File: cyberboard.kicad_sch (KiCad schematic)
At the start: 21 parts, among them J2 Conn_01x06, J4 Lidar, J5 LED, J6 RPi_GPIO, J7 Conn_01x04, J8 Conn_01x03, Q4 AO3400A, U6 ESP32-S3-WROOM-1

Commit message: fix bugs
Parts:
- removed J5: LED, Connector_JST:JST_XH_B3B-XH-A_1x03_P2.50mm_Vertical, symbol Connector_Generic:Conn_01x03
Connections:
- net +3.3V: no longer J6.1 (3.3V), J6.17 (3.3V)
- net CAN_TX: now also U6.17 (GPIO9/TOUCH9/ADC1_CH8/FSPIHD/SUBSPIHD); no longer U6.12 (GPIO8/TOUCH8/ADC1_CH7/SUBSPICS1)
- net FAN: now also J6.8 (BCM14_TXD); no longer J6.11 (BCM17)
- net GPIO_LED: now also U6.12 (GPIO8/TOUCH8/ADC1_CH7/SUBSPICS1); no longer U6.17 (GPIO9/TOUCH9/ADC1_CH8/FSPIHD/SUBSPIHD)
- net MOTORCTL: now also J6.35 (BCM19_MISO_PCM_FS); no longer U6.9 (GPIO16/U0CTS/ADC2_CH5/XTAL_32K_N)
- net UART3_RX: now also U6.37 (U0TXD/GPIO43/CLK_OUT1); no longer U6.36 (U0RXD/GPIO44/CLK_OUT2)
- net UART3_TX: now also U6.36 (U0RXD/GPIO44/CLK_OUT2); no longer U6.37 (U0TXD/GPIO43/CLK_OUT1)
- no-connect marks 16 -> 17
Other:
- moved on the sheet: D1

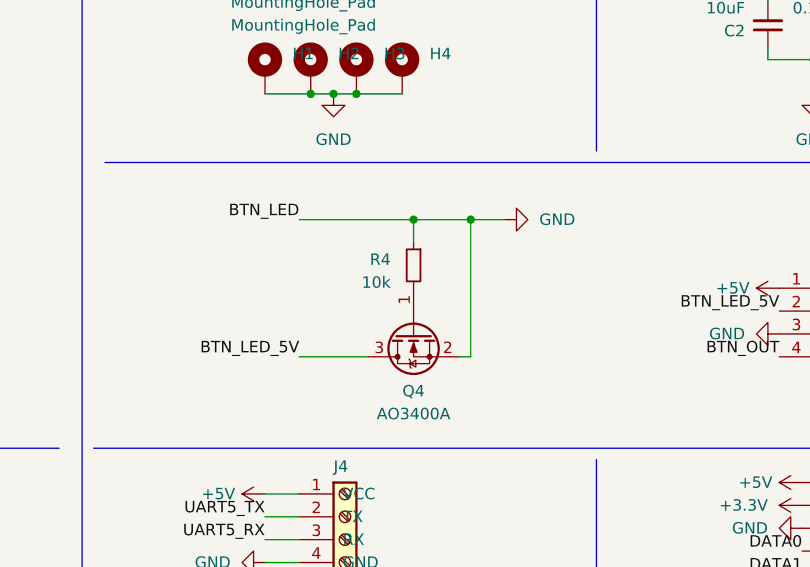
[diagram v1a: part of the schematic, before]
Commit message: fix BTN mosfet connection
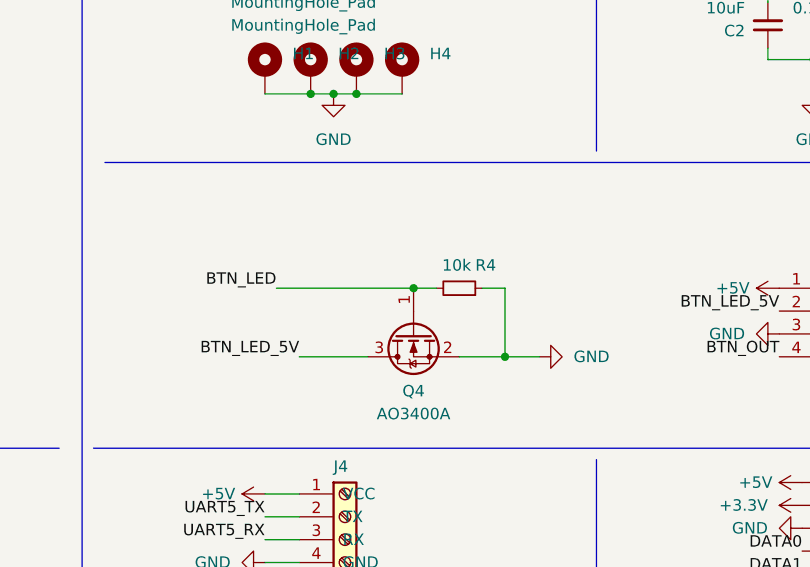
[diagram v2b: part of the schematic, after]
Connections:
- net GND: no longer U6.5 (GPIO5/TOUCH5/ADC1_CH4)
- net BTN_LED: now reaches Q4.1 (G), R4.2
- net BTN_LED: now also U6.5 (GPIO5/TOUCH5/ADC1_CH4)
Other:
- moved on the sheet: R4
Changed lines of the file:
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@@
 	(paper "A4")
 	(junction
-		(at 213.36 95.25)
+		(at 213.36 102.87)
 		(diameter 0)
 		(color 0 0 0 0)
@@
 	)
 	(junction
+		(at 223.52 110.49)
+		(diameter 0)
+		(color 0 0 0 0)
+	)
+	(junction
 		(at 201.93 81.28)
 		(diameter 0)
@@
 		(color 0 0 0 0)
 	)
-	(junction
-		(at 219.71 95.25)
-		(diameter 0)
-		(color 0 0 0 0)
-	)
 	(no_connect
 		(at 142.24 95.25)
@@
 	(wire
 		(pts
+			(xy 215.9 102.87) (xy 213.36 102.87)
+		)
+		(stroke
+			(width 0)
+			(type default)
+		)
+	)
+	(wire
+		(pts
 			(xy 196.85 130.81) (xy 200.66 130.81)
 		)
@@
 	(wire
 		(pts
+			(xy 198.12 102.87) (xy 213.36 102.87)
+		)
+		(stroke
+			(width 0)
+			(type default)
+		)
+	)
+	(wire
+		(pts
 			(xy 252.73 68.58) (xy 252.73 71.12)
 		)
@@
 		)
 	)
+	(wire
+		(pts
+			(xy 223.52 110.49) (xy 227.33 110.49)
+		)
+		(stroke
+			(width 0)
+			(type default)
+		)
+	)
 	(polyline
 		(pts
@@
 	(wire
 		(pts
-			(xy 213.36 95.25) (xy 213.36 97.79)
+			(xy 142.24 29.21) (xy 146.05 29.21)
 		)
 		(stroke
@@
 	(wire
 		(pts
-			(xy 142.24 29.21) (xy 146.05 29.21)
+			(xy 196.85 133.35) (xy 200.66 133.35)
 		)
 		(stroke
@@
 	(wire
 		(pts
-			(xy 196.85 133.35) (xy 200.66 133.35)
+			(xy 220.98 102.87) (xy 223.52 102.87)
 		)
 		(stroke
@@
 		)
 	)
-	(wire
-		(pts
-			(xy 219.71 95.25) (xy 219.71 110.49)
-		)
-		(stroke
-			(width 0)
-			(type default)
-		)
-	)
 	(polyline
 		(pts
@@
 	(wire
 		(pts
-			(xy 257.81 77.47) (xy 257.81 81.28)
+			(xy 223.52 102.87) (xy 223.52 110.49)
 		)
 		(stroke
@@
 	(wire
 		(pts
-			(xy 200.66 95.25) (xy 213.36 95.25)
+			(xy 257.81 77.47) (xy 257.81 81.28)
 		)
 		(stroke
@@
 	(wire
 		(pts
-			(xy 213.36 95.25) (xy 219.71 95.25)
-		)
-		(stroke
-			(width 0)
-			(type default)
-		)
-	)
-	(wire
-		(pts
 			(xy 87.63 142.24) (xy 96.52 142.24)
 		)
@@
 	(wire
 		(pts
-			(xy 218.44 110.49) (xy 219.71 110.49)
-		)
-		(stroke
-			(width 0)
-			(type default)
-		)
-	)
-	(wire
-		(pts
 			(xy 204.47 81.28) (xy 207.01 81.28)
 		)
@@
 	(wire
 		(pts
-			(xy 219.71 95.25) (xy 223.52 95.25)
+			(xy 218.44 110.49) (xy 223.52 110.49)
 		)
 		(stroke
@@
 	)
 	(label "BTN_LED"
-		(at 200.66 95.25 180)
+		(at 198.12 102.87 180)
 		(fields_autoplaced yes)
 		(effects
@@
 	(symbol
 		(lib_id "Device:R_Small")
-		(at 213.36 100.33 0)
-		(mirror y)
+		(at 218.44 102.87 270)
+		(mirror x)
 		(unit 1)
 		(exclude_from_sim no)
@@
 		(dnp no)
 		(property "Reference" "R4"
-			(at 210.82 99.695 0)
+			(at 220.218 100.33 90)
 			(effects
 				(font
@@
 		)
 		(property "Value" "10k"
-			(at 210.82 102.235 0)
+			(at 216.535 100.33 90)
 			(effects
 				(font
@@
 		)
 		(property "Footprint" "Resistor_SMD:R_0805_2012Metric"
-			(at 213.36 100.33 0)
+			(at 218.44 102.87 0)
 			(effects
 				(font
@@
 		)
 		(property "Datasheet" "~"
-			(at 213.36 100.33 0)
+			(at 218.44 102.87 0)
 			(effects
 				(font
@@
 		)
 		(property "Description" ""
-			(at 213.36 100.33 0)
+			(at 218.44 102.87 0)
 			(effects
 				(font
@@
 		)
 		(property "LCSC" "C17414"
-			(at 213.36 100.33 0)
+			(at 218.44 102.87 0)
 			(effects
 				(font
@@
 	(symbol
 		(lib_id "power:GND")
-		(at 223.52 95.25 90)
+		(at 227.33 110.49 90)
 		(unit 1)
 		(exclude_from_sim no)
@@
 		(fields_autoplaced yes)
 		(property "Reference" "#PWR055"
-			(at 229.87 95.25 0)
+			(at 233.68 110.49 0)
 			(effects
 				(font
@@
 		)
 		(property "Value" "GND"
-			(at 227.33 95.2499 90)
+			(at 231.14 110.4899 90)
 			(effects
 				(font
@@
 		)
 		(property "Footprint" ""
-			(at 223.52 95.25 0)
+			(at 227.33 110.49 0)
 			(effects
 				(font
@@
 		)
 		(property "Datasheet" ""
-			(at 223.52 95.25 0)
+			(at 227.33 110.49 0)
 			(effects
 				(font
@@
 		)
 		(property "Description" ""
-			(at 223.52 95.25 0)
+			(at 227.33 110.49 0)
 			(effects
 				(font

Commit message: swap CAN TX/RX
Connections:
- net CAN_RX: now also U6.17 (GPIO9/TOUCH9/ADC1_CH8/FSPIHD/SUBSPIHD); no longer U6.18 (GPIO10/TOUCH10/ADC1_CH9/FSPICS0/FSPIIO4/SUBSPICS0)
- net CAN_TX: now also U6.18 (GPIO10/TOUCH10/ADC1_CH9/FSPICS0/FSPIIO4/SUBSPICS0); no longer U6.17 (GPIO9/TOUCH9/ADC1_CH8/FSPIHD/SUBSPIHD)
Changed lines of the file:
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@@
+		)
+	)
+	(label "CAN_RX"
+		(at 146.05 67.31 0)
+		(fields_autoplaced yes)
+		(effects
+			(font
+				(size 1.27 1.27)
+			)
+			(justify left bottom)
 		)
 	)
@@
 		)
 	)
-	(label "CAN_RX"
-		(at 146.05 69.85 0)
-		(fields_autoplaced yes)
-		(effects
-			(font
-				(size 1.27 1.27)
-			)
-			(justify left bottom)
-		)
-	)
 	(label "MOTORCTL"
 		(at 196.85 135.89 180)
@@
 		)
 	)
-	(label "CAN_TX"
-		(at 146.05 67.31 0)
-		(fields_autoplaced yes)
-		(effects
-			(font
-				(size 1.27 1.27)
-			)
-			(justify left bottom)
-		)
-	)
 	(label "JTAG_MTDI"
 		(at 46.99 49.53 180)
@@
 		)
 	)
+	(label "CAN_TX"
+		(at 146.05 69.85 0)
+		(fields_autoplaced yes)
+		(effects
+			(font
+				(size 1.27 1.27)
+			)
+			(justify left bottom)
+		)
+	)

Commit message: add LED connector and update FAN connector
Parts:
- added D3: D, symbol Device:D
- added J5: Conn_01x03, Connector_JST:JST_XH_B3B-XH-A_1x03_P2.50mm_Vertical, symbol Connector_Generic:Conn_01x03
- added Q6: AO3400A, Package_TO_SOT_SMD:SOT-23, symbol Transistor_FET:AO3400A
- added R6: 10k, Resistor_SMD:R_0805_2012Metric, symbol Device:R_Small
- added R7, R8: 220, Resistor_SMD:R_0805_2012Metric, symbol Device:R_Small
- J8: footprint Connector_JST:JST_XH_B3B-XH-A_1x03_P2.50mm_Vertical -> Connector_JST:JST_XH_B2B-XH-A_1x02_P2.50mm_Vertical; symbol Connector_Generic:Conn_01x03 -> Connector_Generic:Conn_01x02
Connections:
- net +5V: now also D3.1 (K), J5.3 (Pin_3)
- net BTN_LED: now also R8.2; no longer Q4.1 (G), R4.2
- net GND: now also J5.2 (Pin_2), Q6.2 (S), R6.1; no longer J8.2 (Pin_2)
- net at D1.2 (DOUT): now also J5.1 (Pin_1)
- net FAN renamed FAN_PWM
- net FAN_PWM: now also R7.2; no longer J8.3 (Pin_3)
- new net: Q4.1 (G), R4.2, R8.1
- new net: D3.2 (A), J8.2 (Pin_2), Q6.3 (D)
- new net: Q6.1 (G), R6.2, R7.1
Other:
- moved on the sheet: ACTION1

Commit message: add missing part numbers for JLCPCB
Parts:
- D3: LCSC (none) -> C2480
- R8: LCSC C17414 -> C17557
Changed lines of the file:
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@@
 			)
 		)
-		(property "LCSC" "C17414"
+		(property "LCSC" "C17557"
 			(at 204.47 102.87 0)
 			(effects
@@
 			(effects
 				(font
+					(size 1.27 1.27)
+				)
+				(hide yes)
+			)
+		)
+		(property "LCSC" "C2480"
+			(at 194.31 158.75 0)
+			(effects
+				(font

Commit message: fix pcb layout
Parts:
- D3: footprint (none) -> Diode_SMD:D_SOD-323; LCSC C2480 -> C191023
- J5, J8: now left out of the parts list
- R7: LCSC C17414 -> C17557
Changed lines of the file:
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@@
 		(unit 1)
 		(exclude_from_sim no)
-		(in_bom yes)
+		(in_bom no)
 		(on_board yes)
 		(dnp no)
@@
 			)
 		)
-		(property "Footprint" ""
+		(property "Footprint" "Diode_SMD:D_SOD-323"
 			(at 194.31 158.75 0)
 			(effects
@@
 			)
 		)
-		(property "LCSC" "C2480"
+		(property "LCSC" "C191023"
 			(at 194.31 158.75 0)
 			(effects
@@
 			)
 		)
-		(property "LCSC" "C17414"
+		(property "LCSC" "C17557"
 			(at 212.09 151.13 0)
 			(effects
@@
 		(unit 1)
 		(exclude_from_sim no)
-		(in_bom yes)
+		(in_bom no)
 		(on_board yes)
 		(dnp no)
